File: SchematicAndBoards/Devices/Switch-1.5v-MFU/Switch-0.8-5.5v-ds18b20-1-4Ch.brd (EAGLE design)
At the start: 62.4 x 17.8 mm, 18 parts

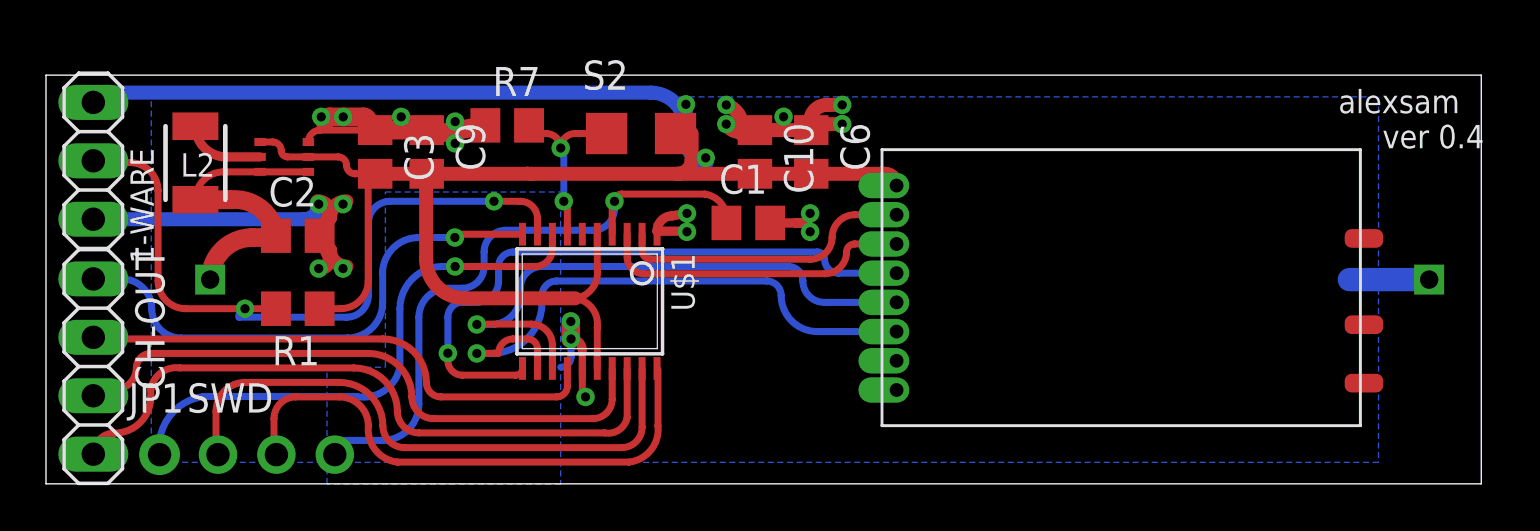
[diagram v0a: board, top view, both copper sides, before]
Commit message: Add Eagle boad and schematic for device Switch-1Ware-4Ch-CC1101-F030F4
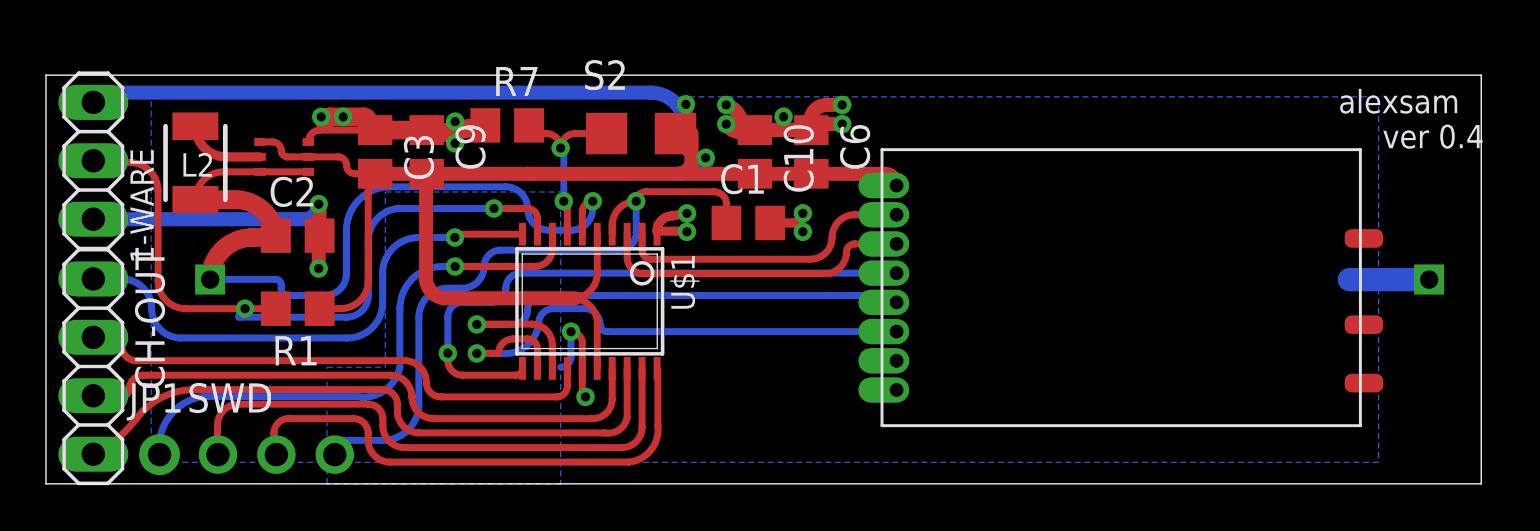
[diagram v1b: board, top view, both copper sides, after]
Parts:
- U$2: value TPS6122 -> TPS61221
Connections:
- net VIN: now also U$1.6
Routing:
- net VIN: track 13.1 -> 36.3 mm, vias 0 -> 1
- net GND: track 53.3 -> 48.2 mm, vias 21 -> 17
- net MISO: track 24.6 -> 22.7 mm
- net MOSI: track 24.8 -> 23.6 mm
- net SCK: track 27.0 -> 25.8 mm
- net NRST: track 27.0 -> 28.1 mm
- net SWCLK: track 23.2 -> 22.2 mm
- net CH_4: track 28.4 -> 27.4 mm
- net SWDIO: track 25.0 -> 24.0 mm
- net 1-WARE: track 31.2 -> 30.5 mm
- net CH_3: track 26.1 -> 25.4 mm

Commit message: Update schematic and boards
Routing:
- net SCK: track 25.8 -> 25.2 mm
- net MISO: track 22.7 -> 22.1 mm
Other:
- board text added: "CLK"
- board text added: "USART"
- board text added: "alexsam @ SaeWave.com"
- board text added: "nRST"
- board text removed: "alexsam"
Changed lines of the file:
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@@
 <?xml version="1.0" encoding="utf-8"?>
 <!DOCTYPE eagle SYSTEM "eagle.dtd">
-<eagle version="7.7.0">
+<eagle version="8.2.1">
 <drawing>
 <settings>
@@
 <layer number="27" name="tValues" color="7" fill="1" visible="no" active="yes"/>
 <layer number="28" name="bValues" color="7" fill="1" visible="no" active="yes"/>
-<layer number="29" name="tStop" color="7" fill="3" visible="no" active="yes"/>
+<layer number="29" name="tStop" color="7" fill="3" visible="yes" active="yes"/>
 <layer number="30" name="bStop" color="7" fill="6" visible="no" active="yes"/>
 <layer number="31" name="tCream" color="7" fill="4" visible="no" active="yes"/>
@@
 <wire x1="62.57" y1="17.77" x2="0.1676" y2="17.77" width="0" layer="20"/>
 <wire x1="0.1676" y1="17.77" x2="0.1676" y2="0" width="0" layer="20"/>
-<text x="56.3576" y="16.114" size="1.016" layer="25" font="vector">alexsam</text>
-<text x="62.6974" y="15.606" size="1.016" layer="25" font="vector" rot="R180">ver 0.4</text>
+<text x="42.3876" y="16.114" size="1.016" layer="25" font="vector">alexsam @ SaeWave.com</text>
+<text x="61.4274" y="15.606" size="1.016" layer="25" font="vector" rot="R180">ver 0.4</text>
+<text x="6.3" y="2.205" size="0.8128" layer="25" rot="R90">USART</text>
+<text x="11.34" y="2.52" size="0.8128" layer="25">nRST</text>
+<text x="10.71" y="2.52" size="0.4064" layer="25" rot="R90">CLK</text>
 </plain>
 <attributes>
@@
 <param name="rvMicroViaOuter" value="0.25"/>
 <param name="rvMicroViaInner" value="0.25"/>
-<param name="rlMinPadTop" value="10mil"/>
+<param name="rlMinPadTop" value="6mil"/>
 <param name="rlMaxPadTop" value="20mil"/>
-<param name="rlMinPadInner" value="10mil"/>
+<param name="rlMinPadInner" value="6mil"/>
 <param name="rlMaxPadInner" value="20mil"/>
-<param name="rlMinPadBottom" value="10mil"/>
+<param name="rlMinPadBottom" value="6mil"/>
 <param name="rlMaxPadBottom" value="20mil"/>
 <param name="rlMinViaOuter" value="8mil"/>
@@
 <param name="mlMinCreamFrame" value="0mil"/>
 <param name="mlMaxCreamFrame" value="0mil"/>
-<param name="mlViaStopLimit" value="0mil"/>
+<param name="mlViaStopLimit" value="25mil"/>
 <param name="srRoundness" value="0"/>
 <param name="srMinRoundness" value="0mil"/>
@@
 <elements>
 <element name="1-WARE" library="pinhead" package="1X03" value="" x="2.225" y="14.045" smashed="yes" rot="R90">
-<attribute name="NAME" x="3.8374" y="14.5878" size="1.016" layer="25" ratio="14" rot="R270"/>
+<attribute name="NAME" x="3.8374" y="15.5228" size="0.8128" layer="25" ratio="14" rot="R270"/>
 <attribute name="VALUE" x="3.225" y="19.045" size="0.8128" layer="27" ratio="10" rot="R180"/>
 </element>
-<element name="C1" library="resistor" package="C0805" value="" x="30.7042" y="11.3428"/>
+<element name="C1" library="resistor" package="C0805" value="" x="30.7042" y="11.3428" smashed="yes">
+<attribute name="NAME" x="30.0642" y="9.4628" size="0.8128" layer="25"/>
+<attribute name="VALUE" x="29.4342" y="8.8028" size="1.27" layer="27"/>
+</element>
 <element name="C10" library="resistor" package="C0805" value="4.7 uF" x="30.99" y="14.43" smashed="yes" rot="R270">
-<attribute name="NAME" x="32.26" y="15.7" size="1.27" layer="25" rot="R270"/>
+<attribute name="NAME" x="29.11" y="15.385" size="0.8128" layer="25" rot="R270"/>
 <attribute name="VALUE" x="29.08" y="15.7" size="1.27" layer="27" rot="R270"/>
 </element>
-<element name="C2" library="resistor" package="C0805" value="" x="11.115" y="10.79"/>
+<element name="C2" library="resistor" package="C0805" value="" x="11.115" y="10.79" smashed="yes">
+<attribute name="NAME" x="10.475" y="12.06" size="0.8128" layer="25"/>
+<attribute name="VALUE" x="9.845" y="8.25" size="1.27" layer="27"/>
+</element>
 <element name="C3" library="resistor" package="C0805" value="" x="14.48" y="14.43" smashed="yes" rot="R90">
-<attribute name="NAME" x="17.02" y="13.16" size="1.27" layer="25" rot="R90"/>
+<attribute name="NAME" x="13.24" y="13.79" size="0.8128" layer="25" rot="R90"/>
 <attribute name="VALUE" x="17.02" y="13.16" size="1.27" layer="27" rot="R90"/>
 </element>
 <element name="C6" library="resistor" package="C0805" value="100 nF" x="33.44" y="14.43" smashed="yes" rot="R270">
-<attribute name="NAME" x="34.71" y="15.7" size="1.27" layer="25" rot="R270"/>
+<attribute name="NAME" x="34.395" y="15.07" size="0.8128" layer="25" rot="R270"/>
 <attribute name="VALUE" x="30.9" y="15.7" size="1.27" layer="27" rot="R270"/>
 </element>
-<element name="C9" library="resistor" package="C0805" value="100 nF" x="16.72" y="14.43" rot="R270"/>
-<element name="CH-OUT" library="pinhead" package="1X04" value="" x="2.225" y="5.1" rot="R270"/>
-<element name="R7" library="resistor" package="R0805" value="" x="20.22" y="15.5854"/>
-<element name="S2" library="my_components" package="1210" value="SET" x="26.04" y="15.23"/>
-<element name="SWD" library="adafruit" package="1X03-CLEANBIG" value="" x="10.185" y="1.27"/>
+<element name="C9" library="resistor" package="C0805" value="100 nF" x="16.72" y="14.43" smashed="yes" rot="R270">
+<attribute name="NAME" x="17.675" y="15.07" size="0.8128" layer="25" rot="R270"/>
+<attribute name="VALUE" x="14.18" y="15.7" size="1.27" layer="27" rot="R270"/>
+</element>
+<element name="CH-OUT" library="pinhead" package="1X04" value="" x="2.225" y="5.1" smashed="yes" rot="R270">
+<attribute name="NAME" x="4.0538" y="7.7162" size="0.8128" layer="25" ratio="10" rot="R270"/>
+<attribute name="VALUE" x="-0.95" y="10.18" size="1.27" layer="27" rot="R270"/>
+</element>
+<element name="R7" library="resistor" package="R0805" value="" x="20.22" y="15.5854" smashed="yes">
+<attribute name="NAME" x="19.585" y="13.7054" size="0.8128" layer="25"/>
+<attribute name="VALUE" x="19.585" y="13.0454" size="1.27" layer="27"/>
+</element>
+<element name="S2" library="my_components" package="1210" value="SET" x="26.04" y="15.23" smashed="yes">
+<attribute name="NAME" x="25.39" y="13.04" size="0.8128" layer="25"/>
+<attribute name="VALUE" x="23.5" y="12.055" size="1.27" layer="27"/>
+</element>
+<element name="SWD" library="adafruit" package="1X03-CLEANBIG" value="" x="10.185" y="1.27" smashed="yes">
+<attribute name="NAME" x="6.9288" y="2.4688" size="0.8128" layer="25" ratio="10"/>
+<attribute name="VALUE" x="6.375" y="-1.905" size="1.27" layer="27"/>
+</element>
 <element name="U$1" library="stm32f030f4" package="TSSOP20" value="STM32F030F4" x="23.81" y="7.935" smashed="yes" rot="R180">
-<attribute name="NAME" x="27.3556" y="10.0178" size="1.016" layer="25" font="vector" ratio="10" rot="R270"/>
 <attribute name="VALUE" x="20.6604" y="7.4374" size="0.6096" layer="27" font="vector" ratio="10"/>
 </element>
 <element name="R1" library="resistor" package="R0805" value="" x="11.115" y="7.615" smashed="yes" rot="R180">
-<attribute name="NAME" x="12.0802" y="6.4212" size="1.27" layer="25" rot="R180"/>
+<attribute name="NAME" x="12.0802" y="6.4212" size="0.8128" layer="25" rot="R180"/>
 <attribute name="VALUE" x="11.75" y="10.155" size="1.27" layer="27" rot="R180"/>
 </element>
@@
 </element>
 <element name="L2" library="SparkFun-Passives" package="1210" value="" x="6.665" y="13.95" smashed="yes" rot="R270">
-<attribute name="NAME" x="6.0174" y="13.3578" size="1.016" layer="25"/>
+<attribute name="NAME" x="6.0174" y="13.3578" size="0.8128" layer="25"/>
 <attribute name="VALUE" x="5.965" y="14.85" size="0.4064" layer="27" rot="R270"/>
 </element>
 <element name="U$3" library="RemoteSwitchComponents" package="AS07-M1101S" value="AS07-M1101S" x="46.675" y="8.88"/>
 <element name="U$4" library="RemoteSwitchComponents" package="BAT-AA1-PCB-HOLDER" value="BAT-AA1-PCB-HOLDER" x="7.305" y="8.88" rot="MR180"/>
-<element name="JP1" library="adafruit" package="1X01-CLEANBIG" value="" x="5.105" y="1.27"/>
+<element name="JP1" library="adafruit" package="1X01-CLEANBIG" value="" x="5.105" y="1.27" smashed="yes">
+<attribute name="VALUE" x="3.835" y="-1.905" size="1.27" layer="27"/>
+</element>
 </elements>
 <signals>
@@
 <wire x1="18.295" y1="7.9" x2="17.64" y2="7.245" width="0.3048" layer="16" curve="90"/>
 <wire x1="17.64" y1="7.245" x2="17.64" y2="5.68" width="0.3048" layer="16"/>
-<wire x1="37.15" y1="9.16" x2="20.815" y2="9.16" width="0.3048" layer="16"/>
+<wire x1="36.515" y1="9.16" x2="20.815" y2="9.16" width="0.3048" layer="16"/>
 <wire x1="20.815" y1="9.16" x2="20.16" y2="8.505" width="0.3048" layer="16" curve="90"/>
 <wire x1="20.16" y1="8.505" x2="19.555" y2="7.9" width="0.3048" layer="16" curve="-90"/>
@@
 <wire x1="22.23" y1="7.62" x2="23.565" y2="7.62" width="0.3048" layer="16"/>
 <wire x1="23.565" y1="7.62" x2="24.255" y2="6.93" width="0.3048" layer="16" curve="-90"/>
-<wire x1="37.15" y1="6.62" x2="24.565" y2="6.62" width="0.3048" layer="16"/>
+<wire x1="36.515" y1="6.62" x2="24.565" y2="6.62" width="0.3048" layer="16"/>
 <wire x1="24.565" y1="6.62" x2="24.255" y2="6.93" width="0.3048" layer="16" curve="-90"/>
 <wire x1="19.965" y1="5.67" x2="19.845" y2="5.675" width="0" layer="19" extent="1-16"/>
@@
 <wire x1="21.105" y1="7.56" x2="21.735" y2="8.19" width="0.3048" layer="16" curve="-90"/>
 <wire x1="21.735" y1="8.19" x2="36.85" y2="8.19" width="0.3048" layer="16"/>
-<wire x1="36.85" y1="8.19" x2="37.15" y2="7.89" width="0.3048" layer="16" curve="-90"/>
+<wire x1="36.85" y1="8.19" x2="36.515" y2="7.89" width="0.3048" layer="16" curve="-90"/>
 </signal>
 <signal name="IRQ">
